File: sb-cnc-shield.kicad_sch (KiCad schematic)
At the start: 62 parts, among them P1 XMOT, P2 YMOT, P3 ZMOT, P4 AMOT, P5 UART, P6 I2C, P7 ES_SETUP, P8 12V-36V, SW1 RESET, U1 ARDUINO_UNO_SHIELD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

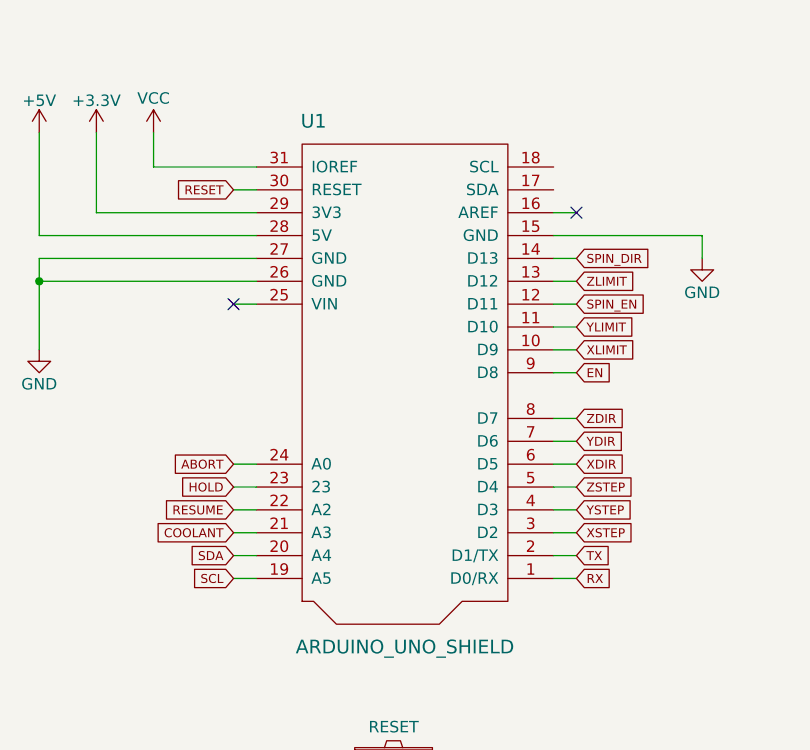
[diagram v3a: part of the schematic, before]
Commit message: use the real scl/sda pins
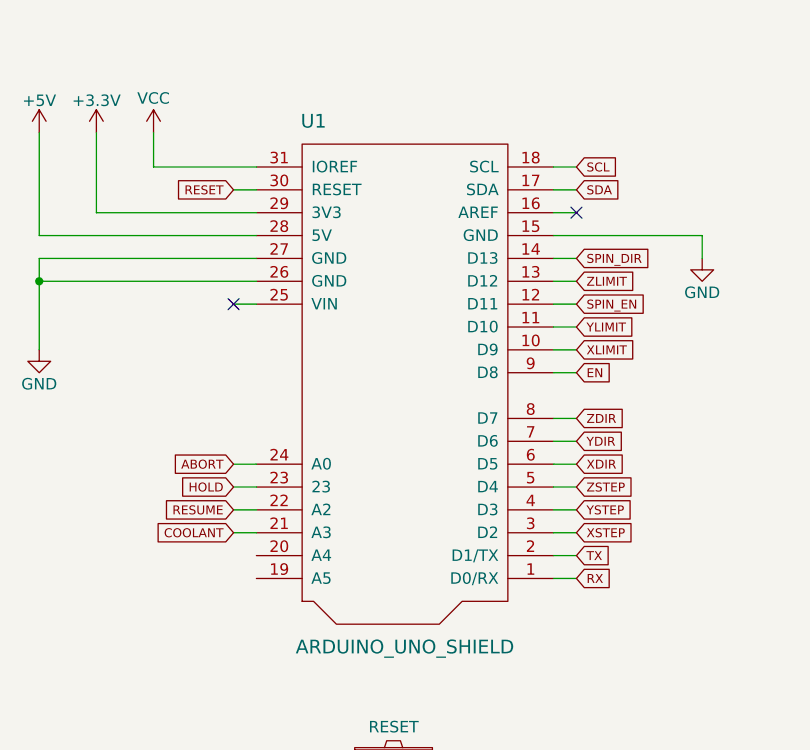
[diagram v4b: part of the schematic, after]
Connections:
- net SCL: now also U1.18 (SCL); no longer U1.19 (A5)
- net SDA: now also U1.17 (SDA); no longer U1.20 (A4)
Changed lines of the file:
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@@
     (stroke (width 0) (type default) (color 0 0 0 0))
   )
+  (wire (pts (xy 82.55 38.1) (xy 85.09 38.1))
+    (stroke (width 0) (type default) (color 0 0 0 0))
+  )
   (wire (pts (xy 275.59 119.38) (xy 275.59 116.84))
     (stroke (width 0) (type default) (color 0 0 0 0))
@@
     (stroke (width 0) (type default) (color 0 0 0 0))
   )
-  (wire (pts (xy 46.99 81.28) (xy 49.53 81.28))
-    (stroke (width 0) (type default) (color 0 0 0 0))
-  )
   (wire (pts (xy 90.17 149.86) (xy 95.25 149.86))
     (stroke (width 0) (type default) (color 0 0 0 0))
@@
     (stroke (width 0) (type default) (color 0 0 0 0))
   )
+  (wire (pts (xy 82.55 35.56) (xy 85.09 35.56))
+    (stroke (width 0) (type default) (color 0 0 0 0))
+  )
   (wire (pts (xy 82.55 66.04) (xy 85.09 66.04))
     (stroke (width 0) (type default) (color 0 0 0 0))
@@
     (stroke (width 0) (type default) (color 0 0 0 0))
   )
-  (wire (pts (xy 46.99 78.74) (xy 49.53 78.74))
-    (stroke (width 0) (type default) (color 0 0 0 0))
-  )
   (wire (pts (xy 129.54 129.54) (xy 133.35 129.54))
     (stroke (width 0) (type default) (color 0 0 0 0))
@@
     )
   )
-  (global_label "SDA" (shape input) (at 46.99 78.74 180) (fields_autoplaced)
-    (effects (font (size 0.9906 0.9906)) (justify right))
-    (property "Intersheet References" "${INTERSHEET_REFS}" (id 0) (at 0 0 0)
-      (effects (font (size 1.27 1.27)) hide)
+  (global_label "SDA" (shape input) (at 85.09 38.1 0) (fields_autoplaced)
+    (effects (font (size 0.9906 0.9906)) (justify left))
+    (property "Intersheet References" "${INTERSHEET_REFS}" (id 0) (at 89.6858 38.0381 0)
+      (effects (font (size 0.9906 0.9906)) (justify left) hide)
     )
   )
@@
     )
   )
-  (global_label "SCL" (shape input) (at 46.99 81.28 180) (fields_autoplaced)
-    (effects (font (size 0.9906 0.9906)) (justify right))
-    (property "Intersheet References" "${INTERSHEET_REFS}" (id 0) (at 0 0 0)
-      (effects (font (size 1.27 1.27)) hide)
+  (global_label "SCL" (shape input) (at 85.09 35.56 0) (fields_autoplaced)
+    (effects (font (size 0.9906 0.9906)) (justify left))
+    (property "Intersheet References" "${INTERSHEET_REFS}" (id 0) (at 89.6386 35.4981 0)
+      (effects (font (size 0.9906 0.9906)) (justify left) hide)
     )
   )
@@
   (symbol (lib_id "power:+5V") (at 25.4 31.75 0) (unit 1)
     (in_bom yes) (on_board yes)
-    (property "Reference" "#PWR?" (id 0) (at 25.4 35.56 0)
+    (property "Reference" "#PWR0114" (id 0) (at 25.4 35.56 0)
       (effects (font (size 1.27 1.27)) hide)
     )
@@
     )
     (path "/162c9947-354e-42e4-8cf3-b34290a8f293"
-      (reference "#PWR?") (unit 1) (value "+5V") (footprint "")
+      (reference "#PWR0114") (unit 1) (value "+5V") (footprint "")
     )
     (path "/00000000-0000-0000-0000-0000564b89a6"

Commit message: more changes
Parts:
- added JP40, JP41: Jumper_NO_Small, Jumper:SolderJumper-2_P1.3mm_Open_Pad1.0x1.5mm, symbol Device:Jumper_NO_Small
- added R6: 1K, Resistor_SMD:R_0805_2012Metric, symbol Device:R
- added R7: 10K, Resistor_SMD:R_0805_2012Metric, symbol Device:R
- JP31: value +5V/GND -> VCC/GND
- P1: value XMOT -> X
- P2: value YMOT -> Y
- P3: value ZMOT -> Z
- P4: value AMOT -> A
- P5: value UART -> Conn_01x05; footprint Pin_Headers:Pin_Header_Straight_1x04 -> Connector_PinHeader_2.54mm:PinHeader_1x05_P2.54mm_Vertical; symbol sb-cnc-shield-rescue:CONN_01X04 -> Connector_Generic:Conn_01x05
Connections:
- net +3V3: now also P5.2 (Pin_2); no longer P5.1 (P1)
- net +5V: now also P5.1 (Pin_1)
- net RX: now also P5.5 (Pin_5); no longer P5.4 (P4)
- net TX: now also P5.4 (Pin_4); no longer P5.3 (P3)
- net VCC: now also P5.3 (Pin_3), R7.1; no longer P5.2 (P2)
- net TMC_RX: now reaches U1.19 (A5)
- net TMC_RX: now also JP41.1
- net TMC_TX: now reaches U1.20 (A4)
- net TMC_TX: now also JP40.1
- net TMC_UART: now reaches U5.5 (RST), U5.6 (SLP)
- net TMC_UART: now also U2.5 (RST), U2.6 (SLP), U3.5 (RST), U3.6 (SLP), U4.5 (RST), U4.6 (SLP), JP41.2, R6.1, R7.2
- new net: JP40.2, R6.2

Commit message: some more small edits
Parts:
- JP40, JP41: footprint Jumper:SolderJumper-2_P1.3mm_Open_Pad1.0x1.5mm -> Jumper:SolderJumper-2_P1.3mm_Open_TrianglePad1.0x1.5mm
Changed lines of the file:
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@@
       (effects (font (size 1.27 1.27)) hide)
     )
-    (property "Footprint" "Jumper:SolderJumper-2_P1.3mm_Open_Pad1.0x1.5mm" (id 2) (at 134.62 172.72 0)
+    (property "Footprint" "Jumper:SolderJumper-2_P1.3mm_Open_TrianglePad1.0x1.5mm" (id 2) (at 134.62 172.72 0)
       (effects (font (size 1.524 1.524)) hide)
     )
@@
       (effects (font (size 1.27 1.27)) hide)
     )
-    (property "Footprint" "Jumper:SolderJumper-2_P1.3mm_Open_Pad1.0x1.5mm" (id 2) (at 134.62 182.88 0)
+    (property "Footprint" "Jumper:SolderJumper-2_P1.3mm_Open_TrianglePad1.0x1.5mm" (id 2) (at 134.62 182.88 0)
       (effects (font (size 1.524 1.524)) hide)
     )
@@
     )
     (path "/848e20a4-557f-4007-8642-e031cee2b4c6"
-      (reference "JP40") (unit 1) (value "Jumper_NO_Small") (footprint "Jumper:SolderJumper-2_P1.3mm_Open_Pad1.0x1.5mm")
+      (reference "JP40") (unit 1) (value "Jumper_NO_Small") (footprint "Jumper:SolderJumper-2_P1.3mm_Open_TrianglePad1.0x1.5mm")
     )
     (path "/b3225d29-f857-4d57-85ef-a8f3aed9bffe"
-      (reference "JP41") (unit 1) (value "Jumper_NO_Small") (footprint "Jumper:SolderJumper-2_P1.3mm_Open_Pad1.0x1.5mm")
+      (reference "JP41") (unit 1) (value "Jumper_NO_Small") (footprint "Jumper:SolderJumper-2_P1.3mm_Open_TrianglePad1.0x1.5mm")
     )
     (path "/00000000-0000-0000-0000-0000564a113b"
